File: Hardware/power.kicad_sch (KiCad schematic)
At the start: 41 parts, among them IC1 TPS54202HDDCR, Q1 SI2347DS-T1-GE3, T1 TP_VCC, T2 TP_GND, T3 TP_VCC, T4 TP_GND, T5 TP_+5V, T6 TP_+3V3, T7 TP_GND, T8 TP_+5V, T9 TP_GND, U1 LM1117-3.3

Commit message: scheme update
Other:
- title: (none) -> PLC ON STM
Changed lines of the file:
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@@
 	(paper "A4")
 	(title_block
+		(title "PLC ON STM")
 		(company "Author: Grzegorz Potocki")
 	)

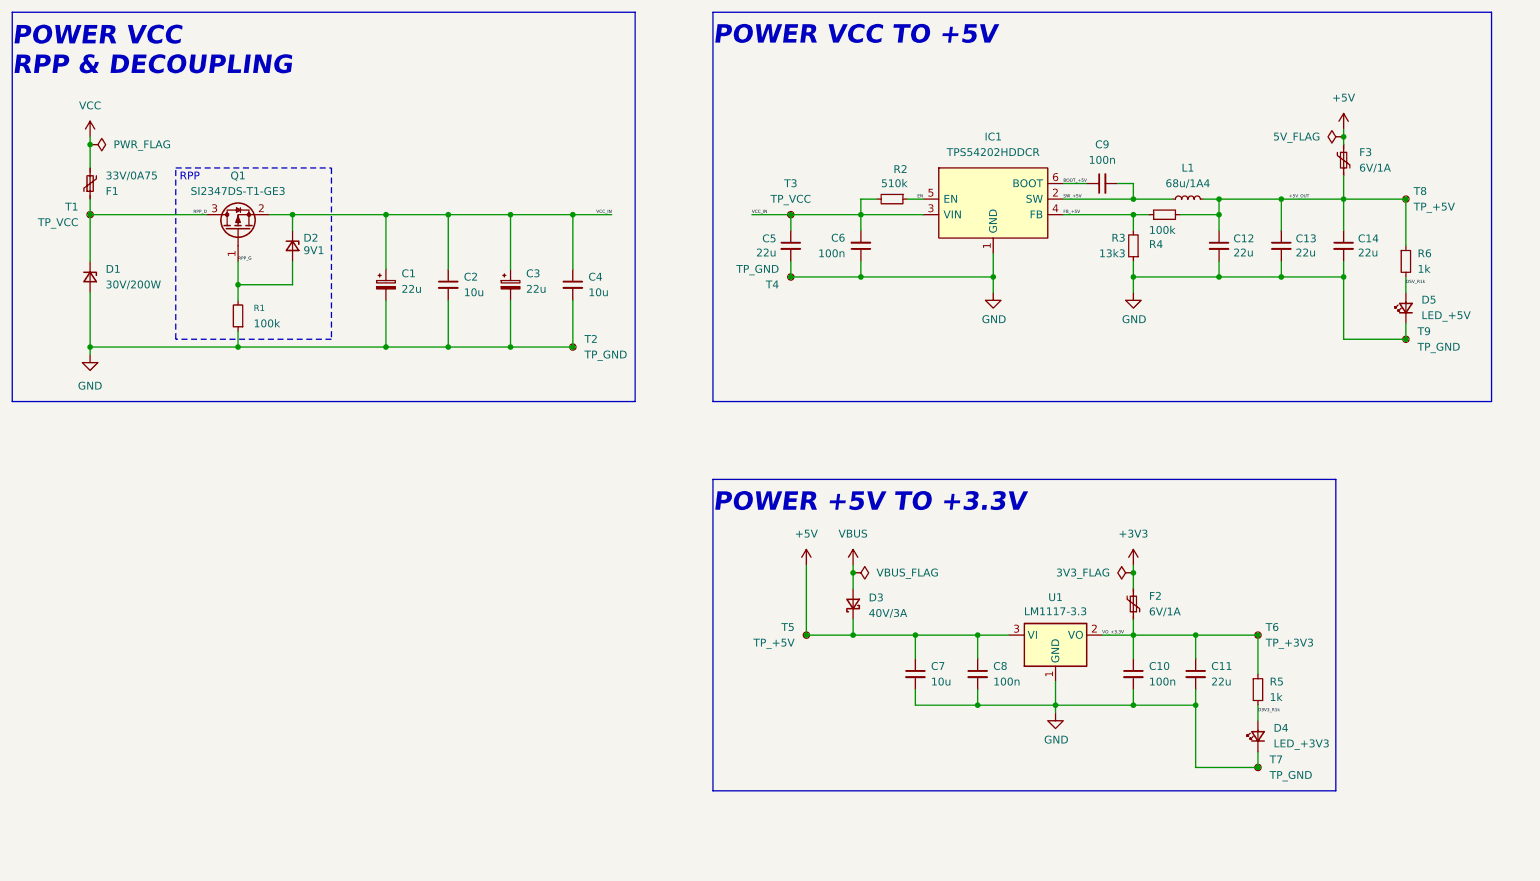
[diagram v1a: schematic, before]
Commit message: schematic update
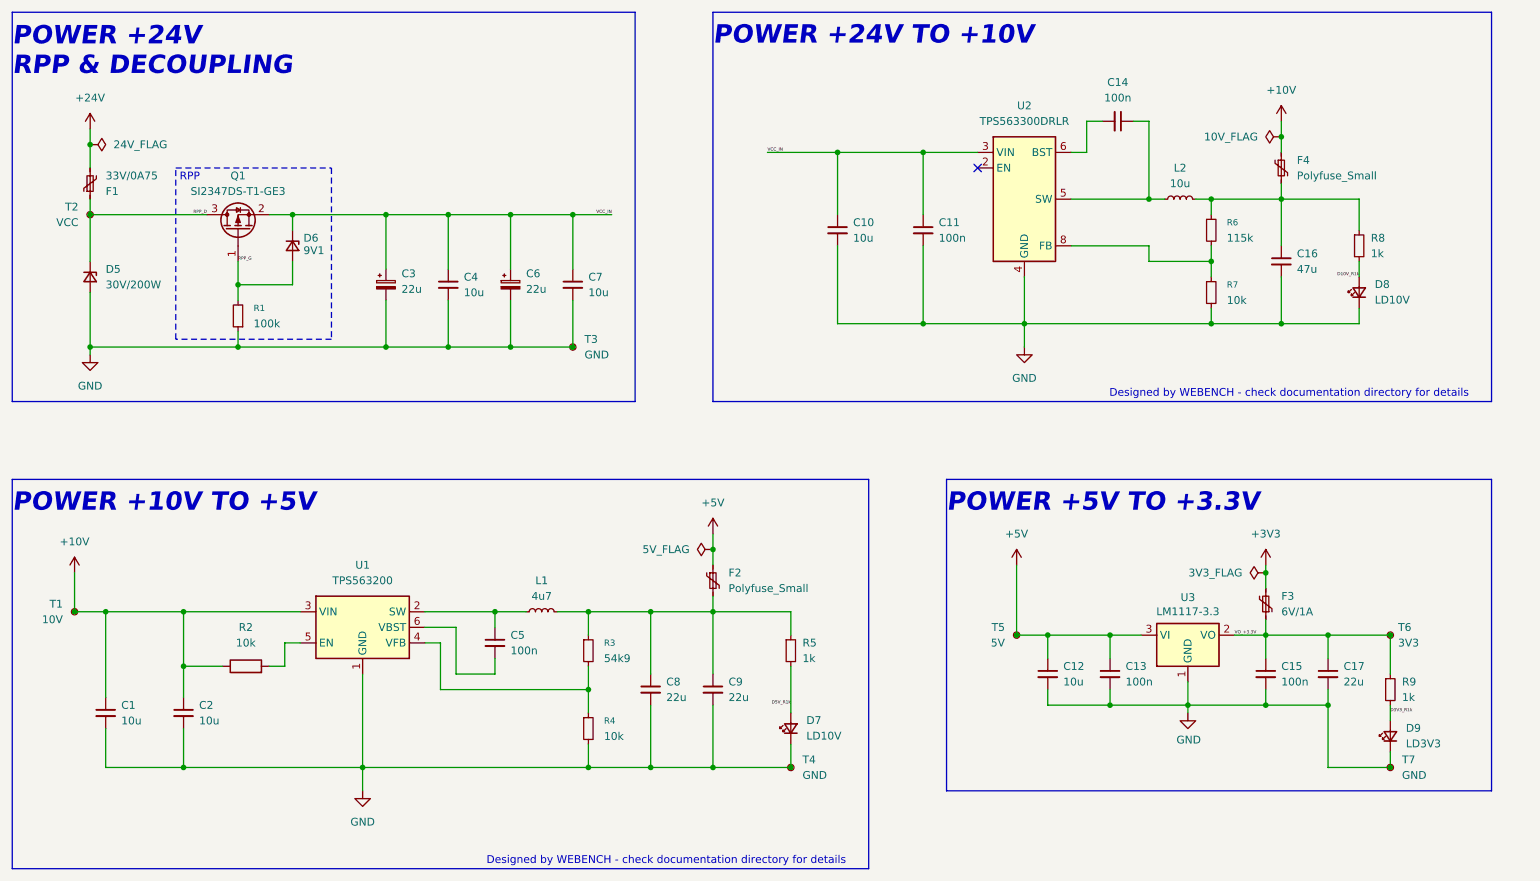
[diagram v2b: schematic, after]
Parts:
- removed C12, C13: 22u, Capacitor_SMD:C_0603_1608Metric_Pad1.08x0.95mm_HandSolder, symbol Device:C_Small
- removed C6: 100n, Capacitor_SMD:C_0603_1608Metric_Pad1.08x0.95mm_HandSolder, symbol Device:C_Small
- removed D3: 40V/3A, Diode_SMD:D_SOD-123F, symbol Device:D_Schottky_Small
- removed D5: LED_+5V, LED_SMD:LED_0603_1608Metric_Pad1.05x0.95mm_HandSolder, symbol Device:LED_Small
- removed F3: 6V/1A, Fuse:Fuse_0805_2012Metric_Pad1.15x1.40mm_HandSolder, symbol Device:Polyfuse_Small
- removed IC1: TPS54202HDDCR, Package_TO_SOT_SMD:SOT-23-6_Handsoldering, symbol SamacsysNew:TPS54202HDDCR
- removed L1: 68u/1A4, Inductor_SMD:L_TDK_VLS6045EX_VLS6045AF, symbol Samacsys_kicad_sym:SRR4028-271Y
- removed R2: 510k, Resistor_SMD:R_0603_1608Metric_Pad0.98x0.95mm_HandSolder, symbol Device:R_Small
- removed T3: TP_VCC, TestPoint:TestPoint_Pad_1.0x1.0mm, symbol Connector:TestPoint_Small
- removed T8: TP_+5V, TestPoint:TestPoint_Pad_1.0x1.0mm, symbol Connector:TestPoint_Small
- removed T9: TP_GND, TestPoint:TestPoint_Pad_1.0x1.0mm, symbol Connector:TestPoint_Small
- added C1, C10, C2: 10u, symbol Device:C_Small
- added C11: 100n, symbol Device:C_Small
- added C16: 47u, symbol Device:C_Small
- added C8: 22u, symbol Device:C_Small
- added D7, D8: LD10V, LED_SMD:LED_0603_1608Metric_Pad1.05x0.95mm_HandSolder, symbol Device:LED_Small
- added F2, F4: Polyfuse_Small, symbol Device:Polyfuse_Small
- added L1: 4u7, symbol Device:L_Small
- added L2: 10u, symbol Device:L_Small
- added R2: 10k, symbol Device:R
- added R5, R8: 1k, Resistor_SMD:R_0603_1608Metric_Pad0.98x0.95mm_HandSolder, symbol Device:R_Small
- added R7: 10k, symbol Device:R_Small
- added T1: 10V, TestPoint:TestPoint_Pad_1.0x1.0mm, symbol Connector:TestPoint_Small
- added U1: TPS563200, Package_TO_SOT_SMD:SOT-23-6, symbol Regulator_Switching:TPS563200
- added U2: TPS563300DRLR, Package_TO_SOT_SMD:SOT-583-8, symbol Regulator_Switching:TPS563300
- C14, C5: value 22u -> 100n; footprint Capacitor_SMD:C_0603_1608Metric_Pad1.08x0.95mm_HandSolder -> (none); Manufacturer_Name MCASH21GCC7684MTCA1J -> (none); Manufacturer_Part_Number CL21A107MQYNNWE -> (none); Mouser Part Number 810-C2012X5R1V226MAC -> (none); Mouser Price/Stock https://www.mouser.pl/ProductDetail/TDK/C2012X5R1V226M125AC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 -> (none)
- C9: value 100n -> 22u; footprint Capacitor_SMD:C_0603_1608Metric_Pad1.08x0.95mm_HandSolder -> (none); Mouser Part Number GRM033R6YA104ME14D -> (none); Mouser Price/Stock https://www.mouser.pl/ProductDetail/Murata-Electronics/GRM0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 -> (none)
- D9: renamed from D4; value LED_+3V3 -> LD3V3
- R3: value 13k3 -> 54k9; footprint Resistor_SMD:R_0603_1608Metric_Pad0.98x0.95mm_HandSolder -> (none); Manufacturer_Name -- -> (none); Manufacturer_Part_Number RT0603DRE0713K3L -> (none); Mouser Part Number 603-RT0603DRE0713K3L -> (none); Mouser Price/Stock https://www.mouser.pl/ProductDetail/YAGEO/RT0603DRE0713K3L?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 -> (none)
- R4: value 100k -> 10k; footprint Resistor_SMD:R_0603_1608Metric_Pad0.98x0.95mm_HandSolder -> (none); Manufacturer_Name -- -> (none); Manufacturer_Part_Number RT0603DRE07100KL -> (none); Mouser Part Number 603-RT0603DRE07100KL -> (none); Mouser Price/Stock https://www.mouser.pl/ProductDetail/KOA-Speer/RK73B1JTTD104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 -> (none)
- R6: value 1k -> 115k; footprint Resistor_SMD:R_0603_1608Metric_Pad0.98x0.95mm_HandSolder -> (none); Mouser Part Number 71-CRCW06031K00FKED -> (none); Mouser Price/Stock https://www.mouser.pl/ProductDetail/Vishay-Dale/CRCW06031K0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 -> (none)
- T2: renamed from T1; value TP_VCC -> VCC
- T3: renamed from T2; value TP_GND -> GND
- T4, T7: value TP_GND -> GND
- T5: value TP_+5V -> 5V
- T6: value TP_+3V3 -> 3V3
- renumbered C7 to C12, C8 to C13, C10 to C15, C11 to C17, C1 to C3, C2 to C4, C3 to C6, C4 to C7, D1 to D5, D2 to D6, F2 to F3, R5 to R9, U1 to U3
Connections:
- net SW_+5V is gone; now on net GND: C9.2
- net +5V: now also F2.1
- net D5V_R1k: now also D7.2 (A), R5.2; no longer R6.2
- net GND: now also R4.2, C1.2, C10.2, C11.2, C16.2, C2.2, C8.2, D7.1 (K), D8.1 (K), R7.2, U1.1 (GND), U2.4 (GND); no longer C14.2, C5.2, R3.1
- net VCC_IN: now also C10.1, C11.1, U2.3 (VIN); no longer C5.1
- removed net +5V_OUT: C14.1, R4.2, R6.1
- net BOOT_+5V: no longer names the net of C9.1
- net BOOT_+5V: now also R3.1, C8.1, F2.2, L1.2, R5.1
- net FB_+5V: no longer names the net of R3.2, R4.1
- net FB_+5V: now also U1.4 (VFB)
- net VCC renamed +24V
- new net: C5.1, L1.1, U1.2 (SW)
- new net: C5.2, U1.6 (VBST)
- new net: C16.1, F4.2, L2.2, R6.1, R8.1
- new net: R2.2, U1.5 (EN)
- new net: C14.1, L2.1, U2.5 (SW)
- new net: C14.2, U2.6 (BST)
- new net: R6.2, R7.1, U2.8 (FB)
- new net +10V: C1.1, C2.1, F4.1, R2.1, T1.1, U1.3 (VIN)
- new net D10V_R1k: D8.2 (A), R8.2
- no-connect marks 0 -> 1
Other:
- note added: "Designed by WEBENCH - check documentation directory for details"
- note added: "POWER +10V TO +5V"
- note added: "POWER +24V RPP & DECOUPLING"
- note added: "POWER +24V TO +10V"
- note removed: "POWER VCC RPP & DECOUPLING"
- note removed: "POWER VCC TO +5V"
- moved on the sheet: C12, C13, C15, C17, D9, F3, R9, T5, T6, T7, U3
